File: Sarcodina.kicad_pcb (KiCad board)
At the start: 2 copper layers, 94 x 94 mm, 375 parts, among them SW1 SW_PUSH, SW10 SW_PUSH, SW11 SW_PUSH, SW12 SW_PUSH, SW13 SW_PUSH, SW14 SW_PUSH, SW15 SW_PUSH, SW16 SW_PUSH, SW17 SW_PUSH, SW18 SW_PUSH, SW19 SW_PUSH, SW2 SW_PUSH, SW20 SW_PUSH, SW21 SW_PUSH, SW22 SW_PUSH, SW23 SW_PUSH, SW24 SW_PUSH, SW25 SW_PUSH, SW3 SW_PUSH, SW4 SW_PUSH, SW5 SW_PUSH, SW6 SW_PUSH, SW7 SW_PUSH, SW8 SW_PUSH, SW9 SW_PUSH

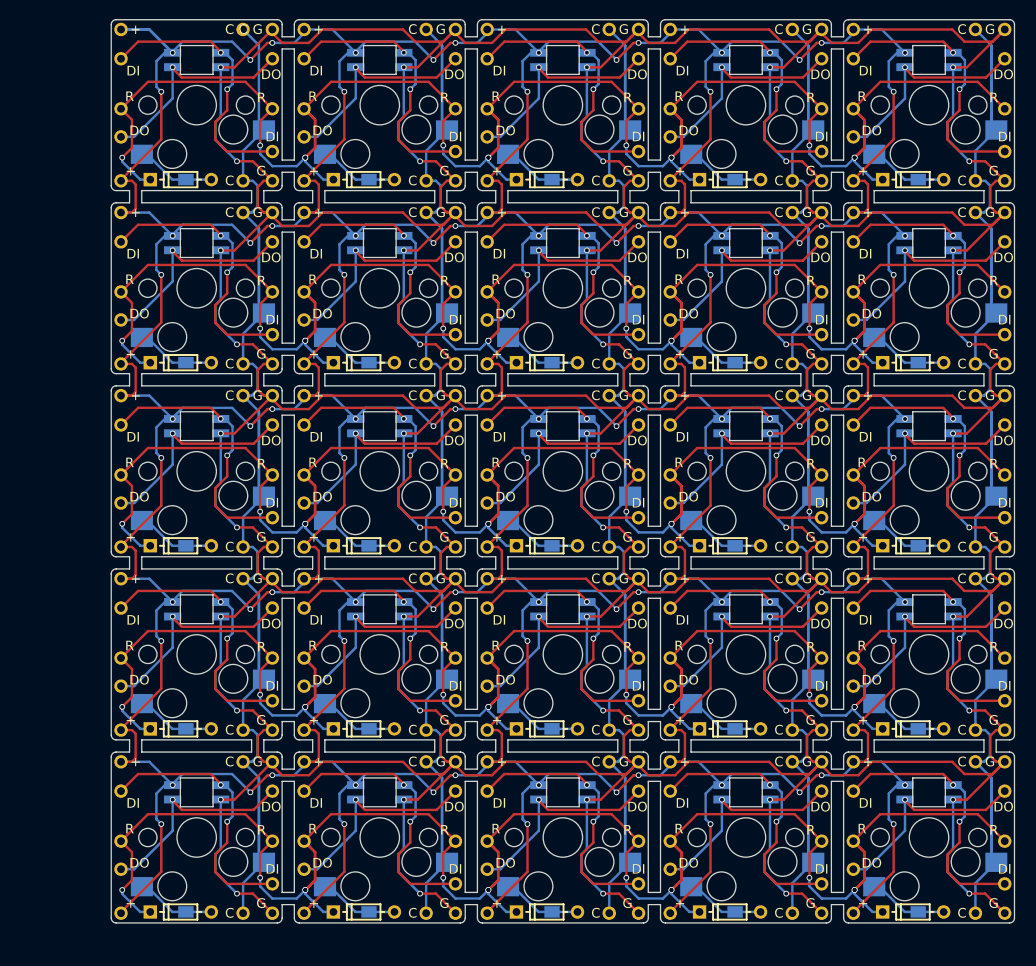
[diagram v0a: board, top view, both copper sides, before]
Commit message: Fixed some warnings produced by dup tracks and vias.
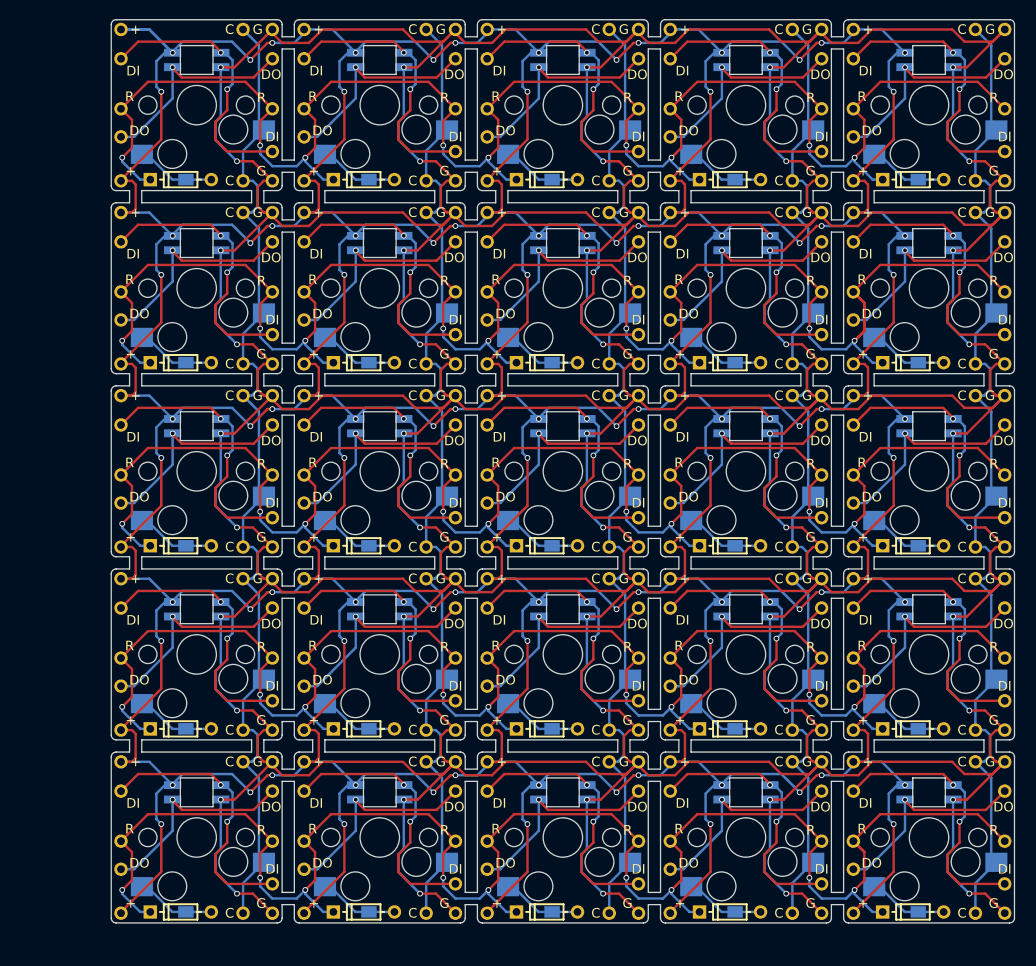
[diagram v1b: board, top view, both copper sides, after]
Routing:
- net col3: track 149.2 -> 110.5 mm
- net col2: track 149.2 -> 110.5 mm
- net col4: track 149.2 -> 110.5 mm
- net col1: track 149.2 -> 110.5 mm
- net col0: track 142.3 -> 111.3 mm
- net row3: track 207.9 -> 184.0 mm, vias 13 -> 9
- net row2: track 207.9 -> 184.0 mm, vias 13 -> 9
- net row0: track 207.9 -> 184.0 mm, vias 13 -> 9
- net row4: track 207.9 -> 185.7 mm, vias 13 -> 9
- net row1: track 207.9 -> 190.0 mm, vias 13 -> 9

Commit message: Changed to a develop branch to update the pcb.
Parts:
- removed ** (x7), **1, **10, **100, **101, **102, **103, **104, **105, **106, **107, **108, **109, **11, **110, **111, **112, **113, **114, **115, **116, **117, **118, **119, **12, **120, **121, **122, **123, **124, **125, **126, **127, **128, **129, **13, **130, **131, **132, **133, **134, **135, **136, **137, **138, **139, **14, **140, **141, **142, **143, **144, **145, **146, **147, **148, **149, **15, **150, **151, **152, **153, **154, **155, **156, **157, **158, **159, **16, **160, **161, **162, **163, **164, **165, **166, **167, **168, **17, **18, **19, **2, **20, **21, **22, **23, **24, **25, **26, **27, **28, **29, **3, **30, **31, **32, **33, **34, **35, **36, **37, **38, **39, **4, **40, **41, **42, **43, **44, **45, **46, **47, **48, **49, **5, **50, **51, **52, **53, **54, **55, **56, **57, **58, **59, **6, **60, **61, **62, **63, **64, **65, **66, **67, **68, **69, **7, **70, **71, **72, **73, **74, **75, **76, **77, **78, **79, **8, **80, **81, **82, **83, **84, **85, **86, **87, **88, **89, **9, **90, **91, **92, **93, **94, **95, **96, **97, **98, **99: Val**, kbd:1pin_conn_no_silkscreen
- removed 1, 10, 11, 12, 13, 14, 15, 16, 17, 18, 19, 2, 20, 21, 22, 23, 24, 25, 26, 27, 28, 29, 3, 30, 31, 32, 33, 34, 35, 36, 37, 38, 39, 4, 40, 41, 42, 43, 44, 45, 46, 47, 48, 49, 5, 50, 51, 52, 53, 54, 55, 56, 57, 58, 59, 6, 60, 61, 62, 63, 64, 65, 66, 67, 68, 69, 7, 70, 71, 72, 73, 74, 75, 76, 77, 78, 79, 8, 80, 81, 82, 83, 84, 85, 86, 87, 88, 89, 9, 90, 91, 92, 93, 94, 95, 96: , 
- removed the ? at (109.7, 49.3)
- removed the ? at (109.7, 30.2)
- removed the ? at (71.6, 30.2)
- removed the ? at (71.6, 49.3)
- removed the ? at (109.7, 106.4)
- removed the ? at (128.8, 49.3)
- removed the ? at (71.6, 68.3)
- removed the ? at (109.7, 87.4)
- removed the ? at (128.8, 30.2)
- removed the ? at (90.7, 106.4)
- removed the ? at (90.7, 30.2)
- removed the ? at (52.6, 49.3)
- removed the ? at (71.6, 87.4)
- removed the ? at (128.8, 87.4)
- removed the ? at (52.6, 87.4)
- removed the ? at (52.6, 35.4)
- removed the ? at (52.6, 68.3)
- removed the ? at (90.7, 68.3)
- removed the ? at (68.3, 35.4)
- removed the ? at (109.7, 68.3)
- removed the ? at (128.8, 68.3)
- removed the ? at (90.7, 87.4)
- removed the ? at (128.8, 106.4)
- removed the ? at (52.6, 38.4)
- removed the ? at (90.7, 49.3)
- removed the ? at (65.3, 27.2)
- removed the ? at (52.6, 106.4)
- removed the ? at (52.6, 30.2)
- removed the ? at (71.6, 106.4)
- removed the D at (131.8, 119.0)
- removed the D at (55.6, 61.8)
- removed the D at (74.7, 119.0)
- removed the D at (93.7, 80.9)
- removed the D at (112.8, 42.8)
- removed the D at (74.7, 80.9)
- removed the D at (74.7, 99.9)
- removed the D at (93.7, 61.8)
- removed the D at (131.8, 42.8)
- removed the D at (112.8, 99.9)
- removed the D at (112.8, 61.8)
- removed the D at (93.7, 119.0)
- removed the D at (55.6, 80.9)
- removed the D at (55.6, 99.9)
- removed the D at (112.8, 119.0)
- removed the D at (93.7, 42.8)
- removed the D at (74.7, 61.8)
- removed the D at (131.8, 80.9)
- removed the D at (55.6, 119.0)
- removed the D at (74.7, 42.8)
- removed the D at (131.8, 61.8)
- removed the D at (112.8, 80.9)
- removed the D at (55.6, 42.8)
- removed the D at (93.7, 99.9)
- removed the D at (131.8, 99.9)
- removed the L1 at (79.5, 30.4)
- removed the L1 at (136.7, 68.5)
- removed the L1 at (79.5, 87.5)
- removed the L1 at (136.7, 49.4)
- removed the L1 at (79.5, 106.6)
- removed the L1 at (98.6, 87.5)
- removed the L1 at (79.5, 49.4)
- removed the L1 at (60.5, 87.5)
- removed the L1 at (79.5, 68.5)
- removed the L1 at (98.6, 49.4)
- removed the L1 at (136.7, 87.5)
- removed the L1 at (98.6, 106.6)
- removed the L1 at (117.6, 68.5)
- removed the L1 at (98.6, 68.5)
- removed the L1 at (136.7, 106.6)
- removed the L1 at (117.6, 106.6)
- removed the L1 at (136.7, 30.4)
- removed the L1 at (60.5, 30.4)
- removed the L1 at (60.5, 68.5)
- removed the L1 at (117.6, 49.4)
- removed the L1 at (117.6, 30.4)
- removed the L1 at (98.6, 30.4)
- removed the L1 at (60.5, 106.6)
- removed the L1 at (60.5, 49.4)
- removed the L1 at (117.6, 87.5)
- removed SW1, SW10, SW11, SW12, SW13, SW14, SW15, SW16, SW17, SW18, SW19, SW2, SW20, SW21, SW22, SW23, SW24, SW25, SW3, SW4, SW5, SW6, SW8, SW9: SW_PUSH, kbd:CherryMX_Hotswap_single_side
- removed the SW7 at (79.5, 54.1)
- added ?: , , F.Cu at (119.5, 74.3)
- added ?: , , F.Cu at (77.6, 90.8)
- added ?: , , F.Cu at (54.9, 83.2)
- added ?: , , F.Cu at (73.8, 106.0)
- added ?: , , F.Cu at (115.7, 112.4)
- added ?: , , F.Cu at (115.7, 102.2)
- added ?: , , F.Cu at (77.6, 64.1)
- added ?: , , F.Cu at (134.7, 42.4)
- added ?: , , F.Cu at (81.4, 106.0)
- added ?: , , F.Cu at (96.6, 36.2)
- added ?: , , F.Cu at (58.5, 83.2)
- added ?: , , F.Cu at (119.5, 71.7)
- added ?: , , F.Cu at (62.4, 121.3)
- added ?: , , F.Cu at (93.0, 83.2)
- added ?: , , F.Cu at (81.4, 52.7)
- added ?: , , F.Cu at (100.5, 36.2)
- added ?: , , F.Cu at (81.4, 95.9)
- added ?: , , F.Cu at (115.7, 29.8)
- added ?: , , F.Cu at (111.9, 48.9)
- added ?: , , F.Cu at (112.0, 45.1)
- added ?: , , F.Cu at (96.6, 42.4)
- added ?: , , F.Cu at (100.5, 90.8)
- added ?: , , F.Cu at (119.5, 83.2)
- added ?: , , F.Cu at (96.6, 80.5)
- added ?: , , F.Cu at (100.5, 71.7)
- added ?: , , F.Cu at (115.7, 36.2)
- added ?: , , F.Cu at (81.4, 48.9)
- added ?: , , F.Cu at (112.0, 83.2)
- added ?: , , F.Cu at (58.5, 109.8)
- added ?: , , F.Cu at (43.3, 87.0)
- added ?: , , F.Cu at (96.6, 33.6)
- added ?: , , F.Cu at (58.5, 71.7)
- added ?: , , F.Cu at (93.0, 121.3)
- added ?: , , F.Cu at (58.5, 64.1)
- added ?: , , F.Cu at (96.6, 106.0)
- added ?: , , F.Cu at (73.9, 83.2)
- added ?: , , F.Cu at (77.6, 109.8)
- added ?: , , F.Cu at (62.4, 55.2)
- added ?: , , F.Cu at (73.8, 29.8)
- added ?: , , F.Cu at (43.3, 57.8)
- added ?: , , F.Cu at (93.0, 45.1)
- added ?: , , F.Cu at (54.7, 48.9)
- added ?: , , F.Cu at (134.7, 55.2)
- added ?: , , F.Cu at (77.6, 55.2)
- added ?: , , F.Cu at (73.9, 121.3)
- added ?: , , F.Cu at (77.6, 80.5)
- added ?: , , F.Cu at (93.0, 64.1)
- added ?: , , F.Cu at (43.3, 121.3)
- added ?: , , F.Cu at (131.1, 64.1)
- added ?: , , F.Cu at (134.7, 109.8)
- added ?: , , F.Cu at (119.5, 45.1)
- added ?: , , F.Cu at (130.9, 29.8)
- added ?: , , F.Cu at (96.6, 29.8)
- added ?: , , F.Cu at (115.7, 87.0)
- added ?: , , F.Cu at (131.1, 83.2)
- added ?: , , F.Cu at (134.7, 99.5)
- added ?: , , F.Cu at (100.5, 95.9)
- added ?: , , F.Cu at (134.7, 36.2)
- added ?: , , F.Cu at (62.4, 106.0)
- added ?: , , F.Cu at (134.7, 93.3)
- added ?: , , F.Cu at (81.4, 83.2)
- added ?: , , F.Cu at (77.6, 99.5)
- added ?: , , F.Cu at (115.7, 109.8)
- added ?: , , F.Cu at (92.8, 106.0)
- added ?: , , F.Cu at (62.4, 36.2)
- added ?: , , F.Cu at (134.7, 33.6)
- added ?: , , F.Cu at (100.5, 83.2)
- added ?: , , F.Cu at (100.5, 67.9)
- added ?: , , F.Cu at (100.5, 114.9)
- added ?: , , F.Cu at (81.4, 76.8)
- added ?: , , F.Cu at (62.4, 57.8)
- added ?: , , F.Cu at (81.4, 38.7)
- added ?: , , F.Cu at (81.4, 29.8)
- added ?: , , F.Cu at (77.6, 33.6)
- added ?: , , F.Cu at (62.4, 71.7)
- added ?: , , F.Cu at (58.5, 106.0)
- added ?: , , F.Cu at (96.6, 74.3)
- added ?: , , F.Cu at (92.8, 87.0)
- added ?: , , F.Cu at (77.6, 112.4)
- added ?: , , F.Cu at (119.5, 67.9)
- added ?: , , F.Cu at (115.7, 45.1)
- added ?: , , F.Cu at (58.5, 29.8)
- added ?: , , F.Cu at (100.5, 64.1)
- added ?: , , F.Cu at (77.6, 36.2)
- added ?: , , F.Cu at (43.3, 106.0)
- added ?: , , F.Cu at (43.3, 76.8)
- added ?: , , F.Cu at (100.5, 45.1)
- added ?: , , F.Cu at (54.9, 64.1)
- added ?: , , F.Cu at (100.5, 102.2)
- added ?: , , F.Cu at (119.5, 36.2)
- added ?: , , F.Cu at (58.5, 102.2)
- added ?: , , F.Cu at (62.4, 29.8)
- added ?: , , F.Cu at (96.6, 83.2)
- added ?: , , F.Cu at (100.5, 121.3)
- added ?: , , F.Cu at (115.7, 93.3)
- added ?: , , F.Cu at (43.3, 45.1)
- added ?: , , F.Cu at (81.4, 57.8)
- added ?: , , F.Cu at (134.7, 102.2)
- added ?: , , F.Cu at (100.5, 57.8)
- added ?: , , F.Cu at (43.3, 36.2)
- added ?: , , F.Cu at (115.7, 99.5)
- added ?: , , F.Cu at (96.6, 67.9)
- added ?: , , F.Cu at (58.5, 87.0)
- added ?: , , F.Cu at (81.4, 67.9)
- added ?: , , F.Cu at (119.5, 87.0)
- added ?: , , F.Cu at (134.7, 71.7)
- added ?: , , F.Cu at (112.0, 102.2)
- added ?: , , F.Cu at (131.1, 121.3)
- added ?: , , F.Cu at (62.4, 114.9)
- added ?: , , F.Cu at (62.4, 76.8)
- added ?: , , F.Cu at (58.5, 74.3)
- added ?: , , F.Cu at (100.5, 76.8)
- added ?: , , F.Cu at (77.6, 52.7)
- added ?: , , F.Cu at (115.7, 61.4)
- added ?: , , F.Cu at (58.5, 36.2)
- added ?: , , F.Cu at (81.4, 90.8)
- added ?: , , F.Cu at (111.9, 106.0)
- added ?: , , F.Cu at (58.5, 80.5)
- added ?: , , F.Cu at (134.7, 118.6)
- added ?: , , F.Cu at (115.7, 48.9)
- added ?: , , F.Cu at (58.5, 52.7)
- added ?: , , F.Cu at (43.3, 38.7)
- added ?: , , F.Cu at (119.5, 52.7)
- added ?: , , F.Cu at (81.4, 102.2)
- added ?: , , F.Cu at (62.4, 45.1)
- added ?: , , F.Cu at (43.3, 55.2)
- added ?: , , F.Cu at (77.6, 29.8)
- added ?: , , F.Cu at (111.9, 87.0)
- added ?: , , F.Cu at (100.5, 87.0)
- added ?: , , F.Cu at (58.5, 99.5)
- added ?: , , F.Cu at (73.9, 45.1)
- added ?: , , F.Cu at (119.5, 57.8)
- added ?: , , F.Cu at (96.6, 52.7)
- added ?: , , F.Cu at (134.7, 83.2)
- added ?: , , F.Cu at (96.6, 99.5)
- added ?: , , F.Cu at (43.3, 33.6)
- added ?: , , F.Cu at (54.7, 67.9)
- added ?: , , F.Cu at (115.7, 33.6)
- added ?: , , F.Cu at (115.7, 74.3)
- added ?: , , F.Cu at (119.5, 33.6)
- added ?: , , F.Cu at (96.6, 45.1)
- added ?: , , F.Cu at (92.8, 48.9)
- added ?: , , F.Cu at (100.5, 93.3)
- added ?: , , F.Cu at (130.9, 106.0)
- added ?: , , F.Cu at (100.5, 112.4)
- added ?: , , F.Cu at (134.7, 87.0)
- added ?: , , F.Cu at (62.4, 83.2)
- added ?: , , F.Cu at (43.3, 83.2)
- added ?: , , F.Cu at (96.6, 121.3)
- added ?: , , F.Cu at (81.4, 112.4)
- added ?: , , F.Cu at (81.4, 114.9)
- added ?: , , F.Cu at (134.7, 121.3)
- added ?: , , F.Cu at (43.3, 52.7)
- added ?: , , F.Cu at (119.5, 114.9)
- added ?: , , F.Cu at (134.7, 29.8)
- added ?: , , F.Cu at (58.5, 118.6)
- added ?: , , F.Cu at (81.4, 45.1)
- added ?: , , F.Cu at (77.6, 74.3)
- added ?: , , F.Cu at (43.3, 67.9)
- added ?: , , F.Cu at (58.5, 45.1)
- added ?: , , F.Cu at (119.5, 112.4)
- added ?: , , F.Cu at (81.4, 55.2)
- added ?: , , F.Cu at (119.5, 90.8)
- added ?: , , F.Cu at (77.6, 48.9)
- added ?: , , F.Cu at (111.9, 29.8)
- added ?: , , F.Cu at (58.5, 121.3)
- added ?: , , F.Cu at (43.3, 74.3)
- added ?: , , F.Cu at (73.8, 48.9)
- added ?: , , F.Cu at (115.7, 118.6)
- added ?: , , F.Cu at (96.6, 61.4)
- added ?: , , F.Cu at (115.7, 42.4)
- added ?: , , F.Cu at (62.4, 38.7)
- added ?: , , F.Cu at (62.4, 90.8)
- added ?: , , F.Cu at (62.4, 52.7)
- added ?: , , F.Cu at (81.4, 74.3)
- added ?: , , F.Cu at (131.1, 102.2)
- added ?: , , F.Cu at (134.7, 67.9)
- added ?: , , F.Cu at (43.3, 64.1)
- added ?: , , F.Cu at (134.7, 112.4)
- added ?: , , F.Cu at (115.7, 64.1)
- added ?: , , F.Cu at (77.6, 42.4)
- added ?: , , F.Cu at (58.5, 93.3)
- added ?: , , F.Cu at (62.4, 102.2)
- added ?: , , F.Cu at (58.5, 33.6)
- added ?: , , F.Cu at (77.6, 118.6)
- added ?: , , F.Cu at (131.1, 45.1)
- added ?: , , F.Cu at (134.7, 74.3)
- added ?: , , F.Cu at (100.5, 55.2)
- added ?: , , F.Cu at (111.9, 67.9)
- added ?: , , F.Cu at (43.3, 114.9)
- added ?: , , F.Cu at (77.6, 83.2)
- added ?: , , F.Cu at (58.5, 112.4)
- added ?: , , F.Cu at (54.7, 106.0)
- added ?: , , F.Cu at (119.5, 76.8)
- added ?: , , F.Cu at (77.6, 102.2)
- added ?: , , F.Cu at (130.9, 67.9)
- added ?: , , F.Cu at (134.7, 48.9)
- added ?: , , F.Cu at (58.5, 67.9)
- added ?: , , F.Cu at (115.7, 55.2)
- added ?: , , F.Cu at (119.5, 102.2)
- added ?: , , F.Cu at (100.5, 29.8)
- added ?: , , F.Cu at (58.5, 48.9)
- added ?: , , F.Cu at (119.5, 38.7)
- added ?: , , F.Cu at (115.7, 83.2)
- added ?: , , F.Cu at (77.6, 71.7)
- added ?: , , F.Cu at (115.7, 67.9)
- added ?: , , F.Cu at (81.4, 109.8)
- added ?: , , F.Cu at (54.9, 102.2)
- added ?: , , F.Cu at (73.8, 87.0)
- added ?: , , F.Cu at (58.5, 61.4)
- added ?: , , F.Cu at (81.4, 121.3)
- added ?: , , F.Cu at (92.8, 29.8)
- added ?: , , F.Cu at (112.0, 121.3)
- added ?: , , F.Cu at (62.4, 112.4)
- added ?: , , F.Cu at (119.5, 55.2)
- added ?: , , F.Cu at (81.4, 64.1)
- added ?: , , F.Cu at (43.3, 112.4)
- added ?: , , F.Cu at (62.4, 64.1)
- added ?: , , F.Cu at (43.3, 29.8)
- added ?: , , F.Cu at (130.9, 87.0)
- added ?: , , F.Cu at (115.7, 71.7)
- added ?: , , F.Cu at (81.4, 93.3)
- added ?: , , F.Cu at (43.3, 102.2)
- added ?: , , F.Cu at (100.5, 38.7)
- added ?: , , F.Cu at (62.4, 67.9)
- added ?: , , F.Cu at (54.7, 29.8)
- added ?: , , F.Cu at (81.4, 33.6)
- added ?: , , F.Cu at (115.7, 106.0)
- added ?: , , F.Cu at (115.7, 52.7)
- added ?: , , F.Cu at (43.3, 71.7)
- added ?: , , F.Cu at (81.4, 36.2)
- added ?: , , F.Cu at (96.6, 87.0)
- added ?: , , F.Cu at (43.3, 93.3)
- added ?: , , F.Cu at (62.4, 87.0)
- added ?: , , F.Cu at (100.5, 33.6)
- added ?: , , F.Cu at (100.5, 48.9)
- added ?: , , F.Cu at (130.9, 48.9)
- added ?: , , F.Cu at (62.4, 33.6)
- added ?: , , F.Cu at (96.6, 112.4)
- added ?: , , F.Cu at (43.3, 109.8)
- added ?: , , F.Cu at (58.5, 55.2)
- added ?: , , F.Cu at (96.6, 109.8)
- added ?: , , F.Cu at (54.7, 87.0)
- added ?: , , F.Cu at (96.6, 90.8)
- added ?: , , F.Cu at (43.3, 90.8)
- added ?: , , F.Cu at (77.6, 45.1)
- added ?: , , F.Cu at (119.5, 121.3)
- added ?: , , F.Cu at (119.5, 64.1)
- added ?: , , F.Cu at (96.6, 118.6)
- added ?: , , F.Cu at (115.7, 90.8)
- added ?: , , F.Cu at (96.6, 71.7)
- added ?: , , F.Cu at (81.4, 87.0)
- added ?: , , F.Cu at (134.7, 61.4)
- added ?: , , F.Cu at (134.7, 90.8)
- added ?: , , F.Cu at (115.7, 80.5)
- added ?: , , F.Cu at (100.5, 52.7)
- added ?: , , F.Cu at (96.6, 55.2)
- added ?: , , F.Cu at (96.6, 48.9)
- added ?: , , F.Cu at (54.9, 121.3)
- added ?: , , F.Cu at (92.8, 67.9)
- added ?: , , F.Cu at (96.6, 102.2)
- added ?: , , F.Cu at (77.6, 87.0)
- added ?: , , F.Cu at (119.5, 93.3)
- added ?: , , F.Cu at (77.6, 67.9)
- added ?: , , F.Cu at (119.5, 29.8)
- added ?: , , F.Cu at (96.6, 64.1)
- added ?: , , F.Cu at (62.4, 74.3)
- added ?: , , F.Cu at (93.0, 102.2)
- added ?: , , F.Cu at (77.6, 93.3)
- added ?: , , F.Cu at (119.5, 95.9)
- added ?: , , F.Cu at (77.6, 106.0)
- added ?: , , F.Cu at (54.9, 45.1)
- added ?: , , F.Cu at (112.0, 64.1)
- added ?: , , F.Cu at (62.4, 109.8)
- added ?: , , F.Cu at (119.5, 48.9)
- added ?: , , F.Cu at (58.5, 90.8)
- added ?: , , F.Cu at (62.4, 95.9)
- added ?: , , F.Cu at (73.9, 102.2)
- added ?: , , F.Cu at (134.7, 106.0)
- added ?: , , F.Cu at (77.6, 121.3)
- added ?: , , F.Cu at (62.4, 93.3)
- added ?: , , F.Cu at (100.5, 106.0)
- added ?: , , F.Cu at (73.8, 67.9)
- added ?: , , F.Cu at (134.7, 45.1)
- added ?: , , F.Cu at (58.5, 42.4)
- added ?: , , F.Cu at (119.5, 106.0)
- added ?: , , F.Cu at (77.6, 61.4)
- added ?: , , F.Cu at (73.9, 64.1)
- added ?: , , F.Cu at (62.4, 48.9)
- added ?: , , F.Cu at (134.7, 80.5)
- added ?: , , F.Cu at (100.5, 109.8)
- added ?: , , F.Cu at (119.5, 109.8)
- added ?: , , F.Cu at (115.7, 121.3)
- added ?: , , F.Cu at (96.6, 93.3)
- added ?: , , F.Cu at (81.4, 71.7)
- added ?: , , F.Cu at (100.5, 74.3)
- added ?: , , F.Cu at (134.7, 64.1)
- added ?: , , F.Cu at (43.3, 95.9)
- added ?: , , F.Cu at (43.3, 48.9)
- added ?: , , F.Cu at (134.7, 52.7)
- added D: D, kbd:D3_hybrid_common_hole, F.Cu at (103.6, 64.2)
- added D: D, kbd:D3_hybrid_common_hole, F.Cu at (65.5, 83.3)
- added D: D, kbd:D3_hybrid_common_hole, F.Cu at (122.7, 64.2)
- added D: D, kbd:D3_hybrid_common_hole, F.Cu at (103.6, 121.4)
- added D: D, kbd:D3_hybrid_common_hole, F.Cu at (46.5, 64.2)
- added D: D, kbd:D3_hybrid_common_hole, F.Cu at (122.7, 121.4)
- added D: D, kbd:D3_hybrid_common_hole, F.Cu at (46.5, 83.3)
- added D: D, kbd:D3_hybrid_common_hole, F.Cu at (84.6, 64.2)
- added D: D, kbd:D3_hybrid_common_hole, F.Cu at (122.7, 83.3)
- added D: D, kbd:D3_hybrid_common_hole, F.Cu at (103.6, 45.2)
- added D: D, kbd:D3_hybrid_common_hole, F.Cu at (84.6, 83.3)
- added D: D, kbd:D3_hybrid_common_hole, F.Cu at (46.5, 121.4)
- added D: D, kbd:D3_hybrid_common_hole, F.Cu at (65.5, 102.3)
- added D: D, kbd:D3_hybrid_common_hole, F.Cu at (46.5, 45.2)
- added D: D, kbd:D3_hybrid_common_hole, F.Cu at (65.5, 45.2)
- added D: D, kbd:D3_hybrid_common_hole, F.Cu at (84.6, 102.3)
- added D: D, kbd:D3_hybrid_common_hole, F.Cu at (65.5, 64.2)
- added D: D, kbd:D3_hybrid_common_hole, F.Cu at (122.7, 102.3)
- added D: D, kbd:D3_hybrid_common_hole, F.Cu at (84.6, 121.4)
- added D: D, kbd:D3_hybrid_common_hole, F.Cu at (103.6, 102.3)
- added D: D, kbd:D3_hybrid_common_hole, F.Cu at (122.7, 45.2)
- added D: D, kbd:D3_hybrid_common_hole, F.Cu at (84.6, 45.2)
- added D: D, kbd:D3_hybrid_common_hole, F.Cu at (103.6, 83.3)
- added D: D, kbd:D3_hybrid_common_hole, F.Cu at (46.5, 102.3)
- added D: D, kbd:D3_hybrid_common_hole, F.Cu at (65.5, 121.4)
- added L1: SK6812MINI, kbd:YS-SK6812MINI-E, B.Cu at (70.0, 51.9)
- added L1: SK6812MINI, kbd:YS-SK6812MINI-E, B.Cu at (127.1, 32.9)
- added L1: SK6812MINI, kbd:YS-SK6812MINI-E, B.Cu at (108.1, 90.0)
- added L1: SK6812MINI, kbd:YS-SK6812MINI-E, B.Cu at (70.0, 109.1)
- added L1: SK6812MINI, kbd:YS-SK6812MINI-E, B.Cu at (108.1, 32.9)
- added L1: SK6812MINI, kbd:YS-SK6812MINI-E, B.Cu at (108.1, 51.9)
- added L1: SK6812MINI, kbd:YS-SK6812MINI-E, B.Cu at (50.9, 51.9)
- added L1: SK6812MINI, kbd:YS-SK6812MINI-E, B.Cu at (50.9, 109.1)
- added L1: SK6812MINI, kbd:YS-SK6812MINI-E, B.Cu at (89.0, 51.9)
- added L1: SK6812MINI, kbd:YS-SK6812MINI-E, B.Cu at (70.0, 71.0)
- added L1: SK6812MINI, kbd:YS-SK6812MINI-E, B.Cu at (127.1, 109.1)
- added L1: SK6812MINI, kbd:YS-SK6812MINI-E, B.Cu at (89.0, 109.1)
- added L1: SK6812MINI, kbd:YS-SK6812MINI-E, B.Cu at (50.9, 90.0)
- added L1: SK6812MINI, kbd:YS-SK6812MINI-E, B.Cu at (89.0, 32.9)
- added L1: SK6812MINI, kbd:YS-SK6812MINI-E, B.Cu at (127.1, 71.0)
- added L1: SK6812MINI, kbd:YS-SK6812MINI-E, B.Cu at (50.9, 32.9)
- added L1: SK6812MINI, kbd:YS-SK6812MINI-E, B.Cu at (89.0, 90.0)
- added L1: SK6812MINI, kbd:YS-SK6812MINI-E, B.Cu at (127.1, 51.9)
- added L1: SK6812MINI, kbd:YS-SK6812MINI-E, B.Cu at (108.1, 71.0)
- added L1: SK6812MINI, kbd:YS-SK6812MINI-E, B.Cu at (50.9, 71.0)
- added L1: SK6812MINI, kbd:YS-SK6812MINI-E, B.Cu at (127.1, 90.0)
- added L1: SK6812MINI, kbd:YS-SK6812MINI-E, B.Cu at (70.0, 90.0)
- added L1: SK6812MINI, kbd:YS-SK6812MINI-E, B.Cu at (108.1, 109.1)
- added L1: SK6812MINI, kbd:YS-SK6812MINI-E, B.Cu at (89.0, 71.0)
- added L1: SK6812MINI, kbd:YS-SK6812MINI-E, B.Cu at (70.0, 32.9)
- added SW7: SW_PUSH, kbd:CherryMX_Hotswap_single_side, F.Cu at (70.0, 113.6)
- added SW7: SW_PUSH, kbd:CherryMX_Hotswap_single_side, F.Cu at (50.9, 56.5)
- added SW7: SW_PUSH, kbd:CherryMX_Hotswap_single_side, F.Cu at (70.0, 75.5)
- added SW7: SW_PUSH, kbd:CherryMX_Hotswap_single_side, F.Cu at (127.1, 113.6)
- added SW7: SW_PUSH, kbd:CherryMX_Hotswap_single_side, F.Cu at (89.0, 37.4)
- added SW7: SW_PUSH, kbd:CherryMX_Hotswap_single_side, F.Cu at (127.1, 56.5)
- added SW7: SW_PUSH, kbd:CherryMX_Hotswap_single_side, F.Cu at (127.1, 75.5)
- added SW7: SW_PUSH, kbd:CherryMX_Hotswap_single_side, F.Cu at (108.1, 37.4)
- added SW7: SW_PUSH, kbd:CherryMX_Hotswap_single_side, F.Cu at (50.9, 94.6)
- added SW7: SW_PUSH, kbd:CherryMX_Hotswap_single_side, F.Cu at (89.0, 75.5)
- added SW7: SW_PUSH, kbd:CherryMX_Hotswap_single_side, F.Cu at (108.1, 94.6)
- added SW7: SW_PUSH, kbd:CherryMX_Hotswap_single_side, F.Cu at (70.0, 56.5)
- added SW7: SW_PUSH, kbd:CherryMX_Hotswap_single_side, F.Cu at (108.1, 56.5)
- added SW7: SW_PUSH, kbd:CherryMX_Hotswap_single_side, F.Cu at (50.9, 37.4)
- added SW7: SW_PUSH, kbd:CherryMX_Hotswap_single_side, F.Cu at (50.9, 75.5)
- added SW7: SW_PUSH, kbd:CherryMX_Hotswap_single_side, F.Cu at (89.0, 113.6)
- added SW7: SW_PUSH, kbd:CherryMX_Hotswap_single_side, F.Cu at (127.1, 37.4)
- added SW7: SW_PUSH, kbd:CherryMX_Hotswap_single_side, F.Cu at (89.0, 56.5)
- added SW7: SW_PUSH, kbd:CherryMX_Hotswap_single_side, F.Cu at (89.0, 94.6)
- added SW7: SW_PUSH, kbd:CherryMX_Hotswap_single_side, F.Cu at (108.1, 75.5)
- added SW7: SW_PUSH, kbd:CherryMX_Hotswap_single_side, F.Cu at (70.0, 94.6)
- added SW7: SW_PUSH, kbd:CherryMX_Hotswap_single_side, F.Cu at (108.1, 113.6)
- added SW7: SW_PUSH, kbd:CherryMX_Hotswap_single_side, F.Cu at (70.0, 37.4)
- added SW7: SW_PUSH, kbd:CherryMX_Hotswap_single_side, F.Cu at (50.9, 113.6)
- added SW7: SW_PUSH, kbd:CherryMX_Hotswap_single_side, F.Cu at (127.1, 94.6)
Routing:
- net GND: track 1096.4 -> 1067.6 mm
- net Net-(D1-Pad2): track 194.6 -> 216.9 mm
- net VCC: track 1001.6 -> 1021.2 mm
- net row1: track 190.0 -> 172.4 mm, vias 9 -> 5
- net row4: track 185.7 -> 170.8 mm, vias 9 -> 5
- net row3: track 184.0 -> 172.4 mm, vias 9 -> 5
- net row0: track 184.0 -> 172.4 mm, vias 9 -> 5
- net row2: track 184.0 -> 172.4 mm, vias 9 -> 5
- net unconnected-(L1-Pad4): track 703.0 -> 708.6 mm
- net col4: track 110.5 -> 115.3 mm
- net col3: track 110.5 -> 115.3 mm
- net col1: track 110.5 -> 115.3 mm
- net col2: track 110.5 -> 115.3 mm
- net unconnected-(L1-Pad2): track 546.1 -> 550.8 mm
- net col0: track 111.3 -> 115.3 mm
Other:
- outline, holes or cut-outs redrawn
